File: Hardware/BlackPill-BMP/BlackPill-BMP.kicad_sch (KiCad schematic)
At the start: 39 parts, among them J1 JTAG, J2 VCC, J3 GND, J4 SWO, J5 GDB_COMM, J6 TVCC, J7 LogicAna, J8 Conn_01x10, J9 Conn_01x11, U1 BlueAndBlackPill, U2 AD8531ARTZ, U3 SRV05-4, U4 TXS0108EPW, U5 SRV05-4

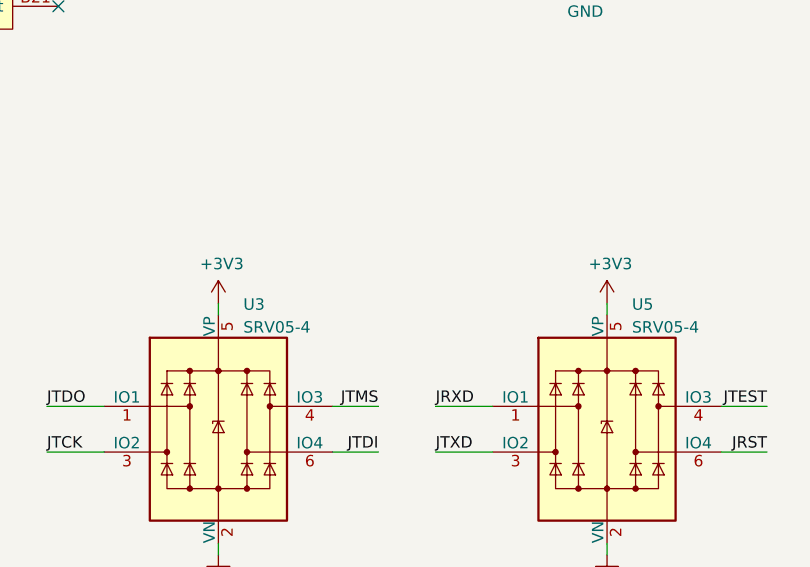
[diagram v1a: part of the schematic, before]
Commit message: Improvements on the ESD circuit.
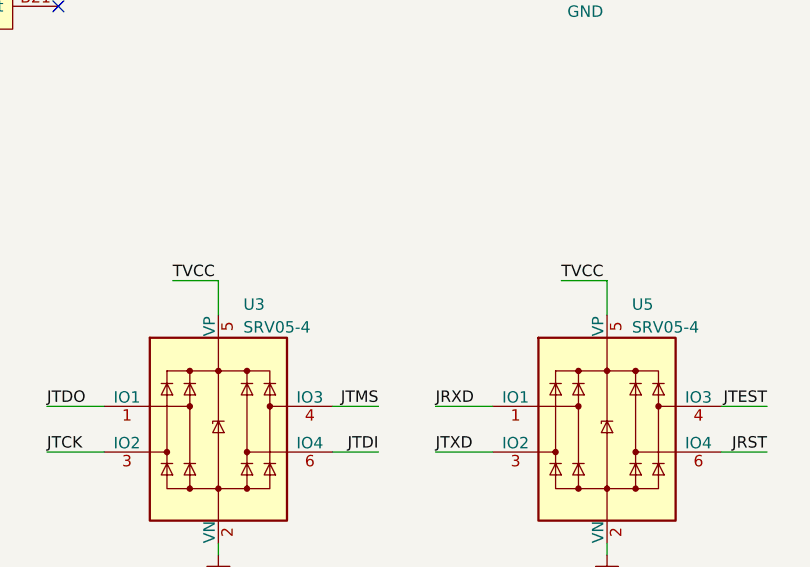
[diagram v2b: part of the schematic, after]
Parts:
- U3, U5: footprint Package_TO_SOT_SMD:SOT-23-6 -> Package_TO_SOT_SMD:SOT-23-6_Handsoldering
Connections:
- net +3V3: no longer U3.5 (VP), U5.5 (VP)
- net TVCC: now also U3.5 (VP), U5.5 (VP)
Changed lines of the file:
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@@
+    (stroke (width 0) (type default) (color 0 0 0 0))
+  )
+  (wire (pts (xy 160.02 104.14) (xy 165.1 104.14))
     (stroke (width 0) (type default) (color 0 0 0 0))
   )
@@
     (stroke (width 0) (type default) (color 0 0 0 0))
   )
+  (wire (pts (xy 208.28 104.14) (xy 203.2 104.14))
+    (stroke (width 0) (type default) (color 0 0 0 0))
+  )
   (wire (pts (xy 20.32 35.56) (xy 26.67 35.56))
     (stroke (width 0) (type default) (color 0 0 0 0))
@@
     (stroke (width 0) (type default) (color 0 0 0 0))
   )
-  (wire (pts (xy 165.1 106.68) (xy 165.1 107.95))
+  (wire (pts (xy 165.1 104.14) (xy 165.1 107.95))
     (stroke (width 0) (type default) (color 0 0 0 0))
   )
@@
     (stroke (width 0) (type default) (color 0 0 0 0))
   )
-  (wire (pts (xy 208.28 106.68) (xy 208.28 107.95))
+  (wire (pts (xy 208.28 104.14) (xy 208.28 107.95))
     (stroke (width 0) (type default) (color 0 0 0 0))
   )
@@
     (effects (font (size 1.27 1.27)) (justify left bottom))
   )
+  (label "TVCC" (at 160.02 104.14 0)
+    (effects (font (size 1.27 1.27)) (justify left bottom))
+  )
   (label "VREF_2" (at 154.94 60.96 180)
     (effects (font (size 1.27 1.27)) (justify right bottom))
   )
   (label "PC13" (at 260.35 115.57 0)
+    (effects (font (size 1.27 1.27)) (justify left bottom))
+  )
+  (label "TVCC" (at 203.2 104.14 0)
     (effects (font (size 1.27 1.27)) (justify left bottom))
   )
@@
   (symbol (lib_id "power:GND") (at 257.81 52.07 0) (mirror y) (unit 1)
     (in_bom yes) (on_board yes)
-    (property "Reference" "#PWR030" (id 0) (at 257.81 58.42 0)
+    (property "Reference" "#PWR028" (id 0) (at 257.81 58.42 0)
       (effects (font (size 1.27 1.27)) hide)
     )
@@
   (symbol (lib_id "power:+3V3") (at 265.43 19.05 0) (unit 1)
     (in_bom yes) (on_board yes)
-    (property "Reference" "#PWR032" (id 0) (at 265.43 22.86 0)
+    (property "Reference" "#PWR030" (id 0) (at 265.43 22.86 0)
       (effects (font (size 1.27 1.27)) hide)
     )
@@
   (symbol (lib_id "power:GND") (at 265.43 33.02 0) (unit 1)
     (in_bom yes) (on_board yes)
-    (property "Reference" "#PWR033" (id 0) (at 265.43 39.37 0)
+    (property "Reference" "#PWR031" (id 0) (at 265.43 39.37 0)
       (effects (font (size 1.27 1.27)) hide)
     )
@@
   (symbol (lib_id "power:GND") (at 264.16 82.55 270) (unit 1)
     (in_bom yes) (on_board yes)
-    (property "Reference" "#PWR031" (id 0) (at 257.81 82.55 0)
+    (property "Reference" "#PWR029" (id 0) (at 257.81 82.55 0)
       (effects (font (size 1.27 1.27)) hide)
     )
@@
       (effects (font (size 1.27 1.27)) (justify left))
     )
-    (property "Footprint" "Package_TO_SOT_SMD:SOT-23-6" (id 2) (at 182.88 132.08 0)
+    (property "Footprint" "Package_TO_SOT_SMD:SOT-23-6_Handsoldering" (id 2) (at 182.88 132.08 0)
       (effects (font (size 1.27 1.27)) hide)
     )
@@
   (symbol (lib_id "power:GND") (at 165.1 134.62 0) (unit 1)
     (in_bom yes) (on_board yes)
-    (property "Reference" "#PWR024" (id 0) (at 165.1 140.97 0)
+    (property "Reference" "#PWR023" (id 0) (at 165.1 140.97 0)
       (effects (font (size 1.27 1.27)) hide)
     )
@@
   (symbol (lib_id "power:GND") (at 205.74 69.85 0) (unit 1)
     (in_bom yes) (on_board yes)
-    (property "Reference" "#PWR026" (id 0) (at 205.74 76.2 0)
+    (property "Reference" "#PWR025" (id 0) (at 205.74 76.2 0)
       (effects (font (size 1.27 1.27)) hide)
     )
@@
     )
     (property "Datasheet" "" (id 3) (at 21.59 73.66 0)
-      (effects (font (size 1.27 1.27)) hide)
-    )
-    (pin "1")
-  )
-  (symbol (lib_id "power:+3V3") (at 165.1 106.68 0) (unit 1)
-    (in_bom yes) (on_board yes)
-    (property "Reference" "#PWR023" (id 0) (at 165.1 110.49 0)
-      (effects (font (size 1.27 1.27)) hide)
-    )
-    (property "Value" "+3V3" (id 1) (at 165.481 102.2858 0))
-    (property "Footprint" "" (id 2) (at 165.1 106.68 0)
-      (effects (font (size 1.27 1.27)) hide)
-    )
-    (property "Datasheet" "" (id 3) (at 165.1 106.68 0)
       (effects (font (size 1.27 1.27)) hide)
     )
@@
   (symbol (lib_id "power:+3V3") (at 208.28 31.75 0) (unit 1)
     (in_bom yes) (on_board yes)
-    (property "Reference" "#PWR027" (id 0) (at 208.28 35.56 0)
+    (property "Reference" "#PWR026" (id 0) (at 208.28 35.56 0)
       (effects (font (size 1.27 1.27)) hide)
     )
@@
       (effects (font (size 1.27 1.27)) (justify left))
     )
-    (property "Footprint" "Package_TO_SOT_SMD:SOT-23-6" (id 2) (at 226.06 132.08 0)
+    (property "Footprint" "Package_TO_SOT_SMD:SOT-23-6_Handsoldering" (id 2) (at 226.06 132.08 0)
       (effects (font (size 1.27 1.27)) hide)
     )
@@
   (symbol (lib_id "power:GND") (at 180.34 50.8 0) (unit 1)
     (in_bom yes) (on_board yes)
-    (property "Reference" "#PWR025" (id 0) (at 180.34 57.15 0)
+    (property "Reference" "#PWR024" (id 0) (at 180.34 57.15 0)
       (effects (font (size 1.27 1.27)) hide)
     )
@@
   (symbol (lib_id "power:GND") (at 208.28 134.62 0) (unit 1)
     (in_bom yes) (on_board yes)
-    (property "Reference" "#PWR029" (id 0) (at 208.28 140.97 0)
+    (property "Reference" "#PWR027" (id 0) (at 208.28 140.97 0)
       (effects (font (size 1.27 1.27)) hide)
     )
@@
     (pin "2")
   )
-  (symbol (lib_id "power:+3V3") (at 208.28 106.68 0) (unit 1)
-    (in_bom yes) (on_board yes)
-    (property "Reference" "#PWR028" (id 0) (at 208.28 110.49 0)
-      (effects (font (size 1.27 1.27)) hide)
-    )
-    (property "Value" "+3V3" (id 1) (at 208.661 102.2858 0))
-    (property "Footprint" "" (id 2) (at 208.28 106.68 0)
-      (effects (font (size 1.27 1.27)) hide)
-    )
-    (property "Datasheet" "" (id 3) (at 208.28 106.68 0)
-      (effects (font (size 1.27 1.27)) hide)
-    )
-    (pin "1")
-  )
   (sheet_instances
     (path "/" (page "1"))
@@
       (reference "#PWR022") (unit 1) (value "GND") (footprint "")
     )
-    (path "/2cf7c132-43df-4e70-9e48-fbfdabf7855d"
-      (reference "#PWR023") (unit 1) (value "+3V3") (footprint "")
-    )
     (path "/177292a1-cad2-4cfc-a234-56280f267644"
+      (reference "#PWR023") (unit 1) (value "GND") (footprint "")
+    )
+    (path "/d4b55beb-06d0-4020-8925-251b91a23438"
       (reference "#PWR024") (unit 1) (value "GND") (footprint "")
     )
-    (path "/d4b55beb-06d0-4020-8925-251b91a23438"
+    (path "/19f890b4-2994-4265-80ed-91ec31d69e55"
       (reference "#PWR025") (unit 1) (value "GND") (footprint "")
     )
-    (path "/19f890b4-2994-4265-80ed-91ec31d69e55"
-      (reference "#PWR026") (unit 1) (value "GND") (footprint "")
-    )
     (path "/56f61c03-f790-48de-9788-53c9d5cdb1d6"
-      (reference "#PWR027") (unit 1) (value "+3V3") (footprint "")
-    )
-    (path "/f531f7c7-6aeb-4777-8d94-d6fb7a19c2fd"
-      (reference "#PWR028") (unit 1) (value "+3V3") (footprint "")
+      (reference "#PWR026") (unit 1) (value "+3V3") (footprint "")
     )
     (path "/e9a7257c-722d-4e7e-a2cf-b7e147247a57"
+      (reference "#PWR027") (unit 1) (value "GND") (footprint "")
+    )
+    (path "/00000000-0000-0000-0000-000061882731"
+      (reference "#PWR028") (unit 1) (value "GND") (footprint "")
+    )
+    (path "/00000000-0000-0000-0000-000061a3cef5"
       (reference "#PWR029") (unit 1) (value "GND") (footprint "")
     )
-    (path "/00000000-0000-0000-0000-000061882731"
-      (reference "#PWR030") (unit 1) (value "GND") (footprint "")
-    )
-    (path "/00000000-0000-0000-0000-000061a3cef5"
+    (path "/00000000-0000-0000-0000-0000618cf4d3"
+      (reference "#PWR030") (unit 1) (value "+3V3") (footprint "")
+    )
+    (path "/00000000-0000-0000-0000-0000618cfb9f"
       (reference "#PWR031") (unit 1) (value "GND") (footprint "")
-    )
-    (path "/00000000-0000-0000-0000-0000618cf4d3"
-      (reference "#PWR032") (unit 1) (value "+3V3") (footprint "")
-    )
-    (path "/00000000-0000-0000-0000-0000618cfb9f"
-      (reference "#PWR033") (unit 1) (value "GND") (footprint "")
     )
     (path "/2261ed48-ebd2-45ce-962e-6715ad8e007f"
@@
     )
     (path "/053d1691-45ec-4891-93ca-09009ba5cb9b"
-      (reference "U3") (unit 1) (value "SRV05-4") (footprint "Package_TO_SOT_SMD:SOT-23-6")
+      (reference "U3") (unit 1) (value "SRV05-4") (footprint "Package_TO_SOT_SMD:SOT-23-6_Handsoldering")
     )
     (path "/e74e0c8f-cd27-41bd-b91e-566b83f9e2d8"
@@
     )
     (path "/700b39c5-43dc-4bc9-bf63-46059e4ca8c6"
-      (reference "U5") (unit 1) (value "SRV05-4") (footprint "Package_TO_SOT_SMD:SOT-23-6")
-    )
-  )
+      (reference "U5") (unit 1) (value "SRV05-4") (footprint "Package_TO_SOT_SMD:SOT-23-6_Handsoldering")
+    )
+  )
